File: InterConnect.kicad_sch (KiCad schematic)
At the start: 2 parts, among them J12 5x2.54mm+2xBus, J5 5x2.54mm+2xBus

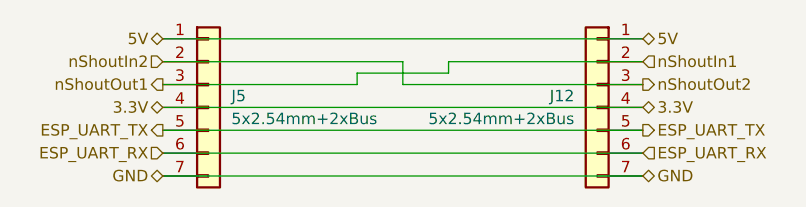
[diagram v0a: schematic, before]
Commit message: Refrences Changed, Root file fixed, UART Note Added
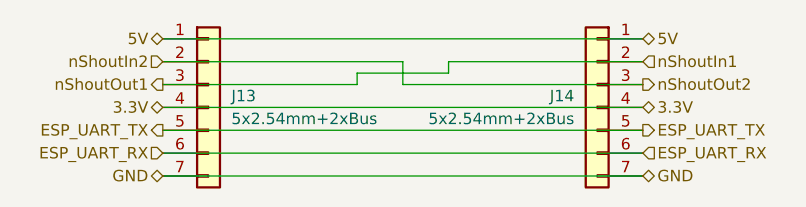
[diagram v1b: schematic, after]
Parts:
- renumbered J5 to J13, J12 to J14
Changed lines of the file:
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@@
 		(dnp no)
 		(fields_autoplaced yes)
-		(property "Reference" "J5"
+		(property "Reference" "J13"
 			(at 123.19 100.3299 0)
 			(effects
@@
 			(project "ECE 2799 Rose Actuator Boards V2"
 				(path "/7b54b20f-95ea-471b-884f-de37eca32e63/59bd2b5d-42f3-4e2d-adcb-a95765ebc7bc"
-					(reference "J5")
+					(reference "J13")
 					(unit 1)
 				)
@@
 		(dnp no)
 		(fields_autoplaced yes)
-		(property "Reference" "J12"
+		(property "Reference" "J14"
 			(at 161.29 100.3299 0)
 			(effects
@@
 			(project "ECE 2799 Rose Actuator Boards V2"
 				(path "/7b54b20f-95ea-471b-884f-de37eca32e63/59bd2b5d-42f3-4e2d-adcb-a95765ebc7bc"
-					(reference "J12")
+					(reference "J14")
 					(unit 1)
 				)
